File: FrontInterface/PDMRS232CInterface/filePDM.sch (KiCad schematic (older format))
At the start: 9 parts

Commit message: PCB Update
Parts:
- renumbered .1 to .?, BP_CAN_IN1 to BP_CAN_IN?, BP_CAN_OUT1 to BP_CAN_OUT?, BP_Power1 to BP_Power?, C13 to C?, C14 to C?, F1 to F?, R4 to R?, R3 to R?
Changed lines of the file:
@@
 EESchema Schematic File Version 4
-LIBS:RS232C Interface-cache
+LIBS:RS232CInterface-cache
 EELAYER 26 0
 EELAYER END
@@
 Connection ~ 3250 3200
 $Comp
-L RS232C-Interface-rescue:CAPACITOR0805-pdm_1-rev0-eagle-import C14
+L RS232C-Interface-rescue:CAPACITOR0805-pdm_1-rev0-eagle-import C?
 U 1 0 DE3531F169098DAB
 P 4750 3400
-F 0 "C14" H 4800 3405 59  0000 L BNN
+F 0 "C?" H 4800 3405 59  0000 L BNN
 F 1 "100n" H 4800 3235 59  0000 L BNN
 F 2 "RS232C-Interface+PDM:Capacitor0805" H 4750 3400 50  0001 C CNN
@@
 $EndComp
 $Comp
-L RS232C-Interface-rescue:RJ45-SOCKET-pdm_1-rev0-eagle-import BP_CAN_OUT1
+L RS232C-Interface-rescue:RJ45-SOCKET-pdm_1-rev0-eagle-import BP_CAN_OUT?
 U 1 0 EC4CBBF8C3190B6C
 P 5450 3300
-F 0 "BP_CAN_OUT1" H 5250 3800 59  0000 L BNN
+F 0 "BP_CAN_OUT?" H 5250 3800 59  0000 L BNN
 F 1 "J" H 5250 2880 59  0000 L BNN
 F 2 "RS232C-Interface+PDM:RJ45-PCB-SOCKET" H 5450 3300 50  0001 C CNN
@@
 $EndComp
 $Comp
-L RS232C-Interface-rescue:HEADER2X4_NORMAL-pdm_1-rev0-eagle-import .1
+L RS232C-Interface-rescue:HEADER2X4_NORMAL-pdm_1-rev0-eagle-import .?
 U 1 0 2E5E96F5F6EEC095
 P 2850 1500
-F 0 ".1" H 2670 1535 59  0000 R TNN
+F 0 ".?" H 2670 1535 59  0000 R TNN
 F 1 "2x4" H 2850 1500 50  0001 C CNN
 F 2 "RS232C-Interface+PDM:Pinheader" H 2850 1500 50  0001 C CNN
@@
 $EndComp
 $Comp
-L RS232C-Interface-rescue:HEADER2X4_NORMAL-pdm_1-rev0-eagle-import .1
+L RS232C-Interface-rescue:HEADER2X4_NORMAL-pdm_1-rev0-eagle-import .?
 U 2 0 2E5E96F5F6EEC099
 P 3250 1500
-F 0 ".1" H 3070 1535 59  0000 R TNN
+F 0 ".?" H 3070 1535 59  0000 R TNN
 F 1 "2x4" H 3250 1500 50  0001 C CNN
 F 2 "RS232C-Interface+PDM:Pinheader" H 3250 1500 50  0001 C CNN
@@
 $EndComp
 $Comp
-L RS232C-Interface-rescue:HEADER2X4_NORMAL-pdm_1-rev0-eagle-import .1
+L RS232C-Interface-rescue:HEADER2X4_NORMAL-pdm_1-rev0-eagle-import .?
 U 3 0 2E5E96F5F6EEC09D
 P 2850 2000
-F 0 ".1" H 2670 2035 59  0000 R TNN
+F 0 ".?" H 2670 2035 59  0000 R TNN
 F 1 "2x4" H 2850 2000 50  0001 C CNN
 F 2 "RS232C-Interface+PDM:Pinheader" H 2850 2000 50  0001 C CNN
@@
 $EndComp
 $Comp
-L RS232C-Interface-rescue:HEADER2X4_NORMAL-pdm_1-rev0-eagle-import .1
+L RS232C-Interface-rescue:HEADER2X4_NORMAL-pdm_1-rev0-eagle-import .?
 U 4 0 2E5E96F5F6EEC081
 P 3250 2000
-F 0 ".1" H 3070 2035 59  0000 R TNN
+F 0 ".?" H 3070 2035 59  0000 R TNN
 F 1 "2x4" H 3250 2000 50  0001 C CNN
 F 2 "RS232C-Interface+PDM:Pinheader" H 3250 2000 50  0001 C CNN
@@
 $EndComp
 $Comp
-L RS232C-Interface-rescue:HEADER2X4_NORMAL-pdm_1-rev0-eagle-import .1
+L RS232C-Interface-rescue:HEADER2X4_NORMAL-pdm_1-rev0-eagle-import .?
 U 5 0 2E5E96F5F6EEC085
 P 2850 2700
-F 0 ".1" H 2670 2735 59  0000 R TNN
+F 0 ".?" H 2670 2735 59  0000 R TNN
 F 1 "2x4" H 2850 2700 50  0001 C CNN
 F 2 "RS232C-Interface+PDM:Pinheader" H 2850 2700 50  0001 C CNN
@@
 $EndComp
 $Comp
-L RS232C-Interface-rescue:HEADER2X4_NORMAL-pdm_1-rev0-eagle-import .1
+L RS232C-Interface-rescue:HEADER2X4_NORMAL-pdm_1-rev0-eagle-import .?
 U 6 0 2E5E96F5F6EEC089
 P 3250 2700
-F 0 ".1" H 3070 2735 59  0000 R TNN
+F 0 ".?" H 3070 2735 59  0000 R TNN
 F 1 "2x4" H 3250 2700 50  0001 C CNN
 F 2 "RS232C-Interface+PDM:Pinheader" H 3250 2700 50  0001 C CNN
@@
 $EndComp
 $Comp
-L RS232C-Interface-rescue:HEADER2X4_NORMAL-pdm_1-rev0-eagle-import .1
+L RS232C-Interface-rescue:HEADER2X4_NORMAL-pdm_1-rev0-eagle-import .?
 U 7 0 2E5E96F5F6EEC08D
 P 2850 3200
-F 0 ".1" H 2670 3235 59  0000 R TNN
+F 0 ".?" H 2670 3235 59  0000 R TNN
 F 1 "2x4" H 2850 3200 50  0001 C CNN
 F 2 "RS232C-Interface+PDM:Pinheader" H 2850 3200 50  0001 C CNN
@@
 $EndComp
 $Comp
-L RS232C-Interface-rescue:HEADER2X4_NORMAL-pdm_1-rev0-eagle-import .1
+L RS232C-Interface-rescue:HEADER2X4_NORMAL-pdm_1-rev0-eagle-import .?
 U 8 0 2E5E96F5F6EEC0B1
 P 3250 3200
-F 0 ".1" H 3070 3235 59  0000 R TNN
+F 0 ".?" H 3070 3235 59  0000 R TNN
 F 1 "2x4" H 3250 3200 50  0001 C CNN
 F 2 "RS232C-Interface+PDM:Pinheader" H 3250 3200 50  0001 C CNN
@@
 $EndComp
 $Comp
-L RS232C-Interface-rescue:RESISTOR2010-pdm_1-rev0-eagle-import R3
+L RS232C-Interface-rescue:RESISTOR2010-pdm_1-rev0-eagle-import R?
 U 1 0 F977EDFF0ED61F71
 P 3050 1100
-F 0 "R3" H 2930 1245 59  0000 L BNN
+F 0 "R?" H 2930 1245 59  0000 L BNN
 F 1 "120R 0.25W" H 2930 1155 59  0000 L BNN
 F 2 "RS232C-Interface+PDM:Resistor-1206" H 3050 1100 50  0001 C CNN
@@
 $EndComp
 $Comp
-L RS232C-Interface-rescue:RESISTOR2010-pdm_1-rev0-eagle-import R4
+L RS232C-Interface-rescue:RESISTOR2010-pdm_1-rev0-eagle-import R?
 U 1 0 C80C4EE536D02DE4
 P 3050 3600
-F 0 "R4" H 2930 3645 59  0000 L BNN
+F 0 "R?" H 2930 3645 59  0000 L BNN
 F 1 "120R 0.25W" H 2930 3485 59  0000 L BNN
 F 2 "RS232C-Interface+PDM:Resistor-1206" H 3050 3600 50  0001 C CNN
@@
 $EndComp
 $Comp
-L RS232C-Interface-rescue:CAPACITOR0805-pdm_1-rev0-eagle-import C13
+L RS232C-Interface-rescue:CAPACITOR0805-pdm_1-rev0-eagle-import C?
 U 1 0 5902D293218CB388
 P 4700 2200
-F 0 "C13" H 4750 2205 59  0000 L BNN
+F 0 "C?" H 4750 2205 59  0000 L BNN
 F 1 "100n" H 4750 2035 59  0000 L BNN
 F 2 "RS232C-Interface+PDM:Capacitor0805" H 4700 2200 50  0001 C CNN
@@
 $EndComp
 $Comp
-L RS232C-Interface-rescue:TERMINAL-2-7.5X10.5MM-pdm_1-rev0-eagle-import BP_Power1
+L RS232C-Interface-rescue:TERMINAL-2-7.5X10.5MM-pdm_1-rev0-eagle-import BP_Power?
 U 1 0 6CFE1E7432EEE89C
 P 1400 2400
-F 0 "BP_Power1" V 1165 2600 59  0000 R TNN
+F 0 "BP_Power?" V 1165 2600 59  0000 R TNN
 F 1 "TERMINAL-2-2,5X5,5MM" H 1400 2400 50  0001 C CNN
 F 2 "RS232C-Interface+PDM:Screwterminal" H 1400 2400 50  0001 C CNN
@@
 Connection ~ 5050 2100
 $Comp
-L RS232C-Interface-rescue:RJ45-SOCKET-pdm_1-rev0-eagle-import BP_CAN_IN1
+L RS232C-Interface-rescue:RJ45-SOCKET-pdm_1-rev0-eagle-import BP_CAN_IN?
 U 1 0 647B296798085B15
 P 5450 2100
-F 0 "BP_CAN_IN1" H 5250 2600 59  0000 L BNN
+F 0 "BP_CAN_IN?" H 5250 2600 59  0000 L BNN
 F 1 "J" H 5250 1680 59  0000 L BNN
 F 2 "RS232C-Interface+PDM:RJ45-PCB-SOCKET" H 5450 2100 50  0001 C CNN
@@
 +24V
 $Comp
-L Device:Fuse F1
+L Device:Fuse F?
 U 1 1 5DCC2090
 P 1000 2550
-F 0 "F1" V 1060 2596 50  0000 L CNN
+F 0 "F?" V 1060 2596 50  0000 L CNN
 F 1 "Fuse" V 1060 2505 50  0000 R CNN
 F 2 "RS232C-Interface+PDM:Fuseholder" V 930 2550 50  0001 C CNN

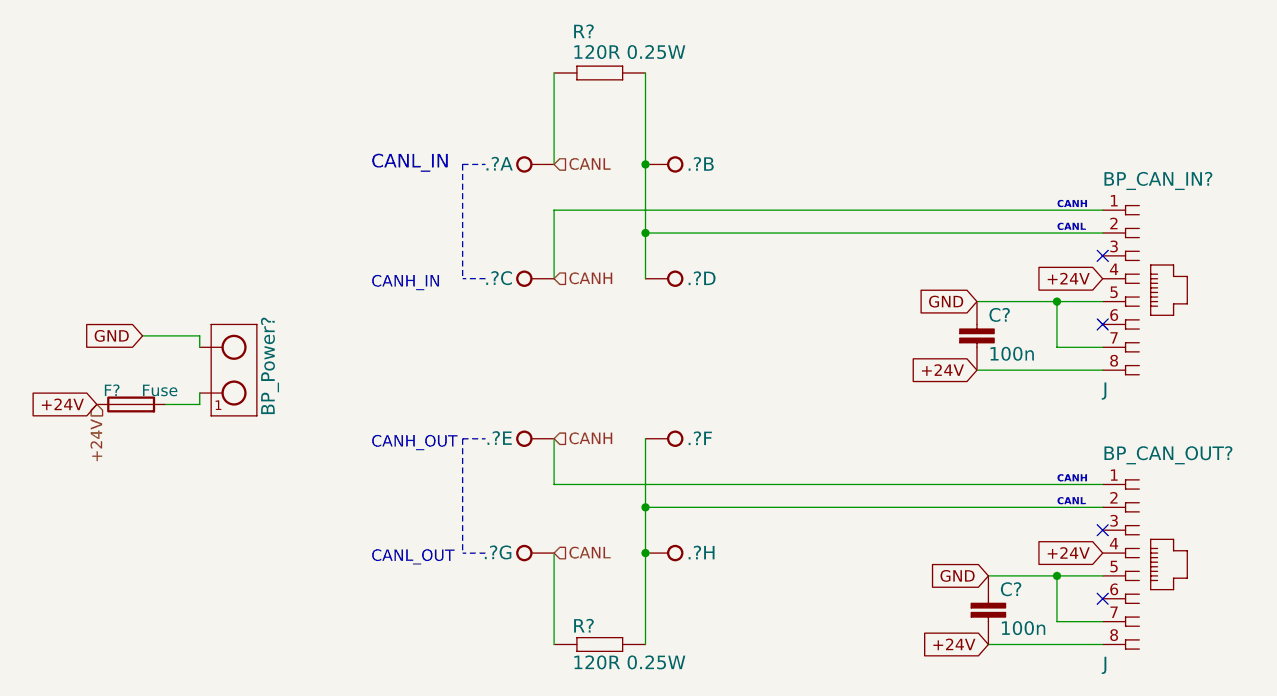
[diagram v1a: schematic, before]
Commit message: PCB updated, Lever Shifter added
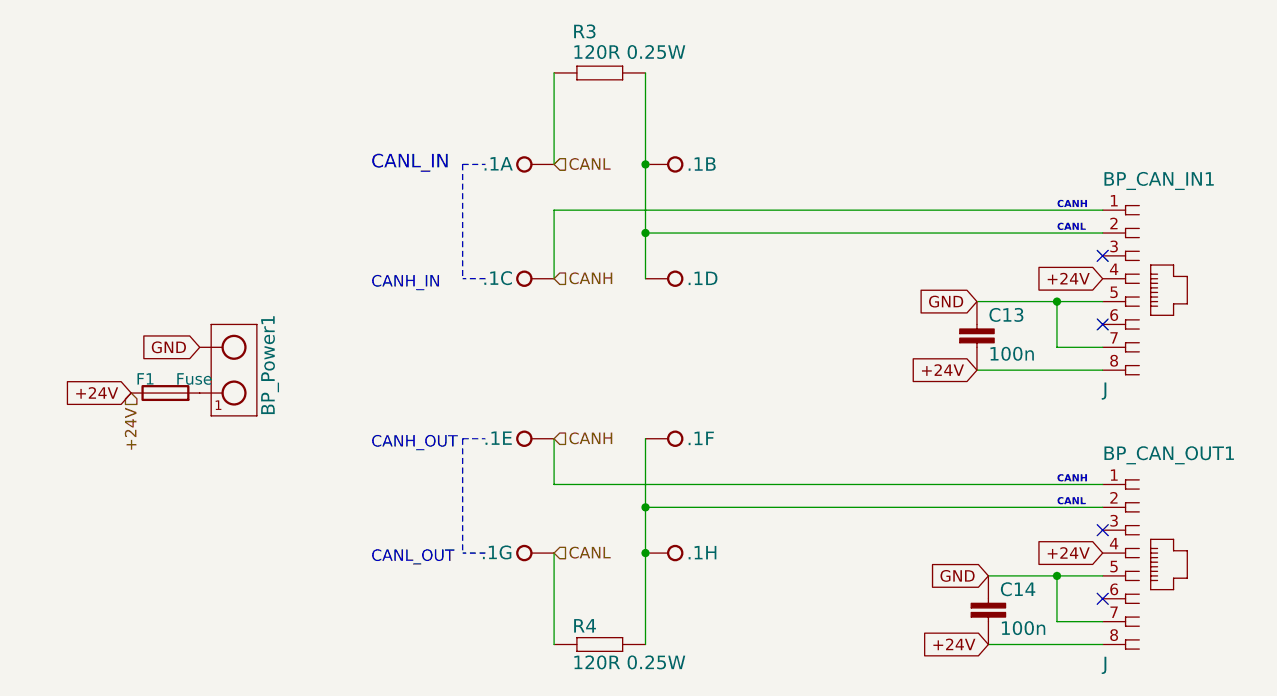
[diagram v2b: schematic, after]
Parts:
- removed .?: 2x4, RS232C-Interface+PDM:Pinheader, symbol RS232C-Interface-rescue:HEADER2X4_NORMAL-pdm_1-rev0-eagle-import
- added unit 3 of .1
- BP_CAN_IN1: renamed from BP_CAN_IN?; footprint RS232C-Interface+PDM:RJ45-PCB-SOCKET -> Connector_RJ:RJ45_Amphenol_54602-x08_Horizontal
- BP_CAN_OUT1: renamed from BP_CAN_OUT?; footprint RS232C-Interface+PDM:RJ45-PCB-SOCKET -> Connector_RJ:RJ45_Amphenol_54602-x08_Horizontal
- gave numbers to parts that had none: 7
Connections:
- net CANH: now also .1.3 (S)
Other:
- moved on the sheet: F1
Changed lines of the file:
@@
 Connection ~ 3250 3200
 $Comp
-L RS232C-Interface-rescue:CAPACITOR0805-pdm_1-rev0-eagle-import C?
+L RS232C-Interface-rescue:CAPACITOR0805-pdm_1-rev0-eagle-import C14
 U 1 0 DE3531F169098DAB
 P 4750 3400
-F 0 "C?" H 4800 3405 59  0000 L BNN
+F 0 "C14" H 4800 3405 59  0000 L BNN
 F 1 "100n" H 4800 3235 59  0000 L BNN
 F 2 "RS232C-Interface+PDM:Capacitor0805" H 4750 3400 50  0001 C CNN
@@
 $EndComp
 $Comp
-L RS232C-Interface-rescue:RJ45-SOCKET-pdm_1-rev0-eagle-import BP_CAN_OUT?
+L RS232C-Interface-rescue:RJ45-SOCKET-pdm_1-rev0-eagle-import BP_CAN_OUT1
 U 1 0 EC4CBBF8C3190B6C
 P 5450 3300
-F 0 "BP_CAN_OUT?" H 5250 3800 59  0000 L BNN
+F 0 "BP_CAN_OUT1" H 5250 3800 59  0000 L BNN
 F 1 "J" H 5250 2880 59  0000 L BNN
-F 2 "RS232C-Interface+PDM:RJ45-PCB-SOCKET" H 5450 3300 50  0001 C CNN
+F 2 "Connector_RJ:RJ45_Amphenol_54602-x08_Horizontal" H 5450 3300 50  0001 C CNN
 F 3 "https://de.rs-online.com/web/p/products/2400935/" H 5450 3300 50  0001 C CNN
 	1    5450 3300
@@
 $EndComp
 $Comp
-L RS232C-Interface-rescue:HEADER2X4_NORMAL-pdm_1-rev0-eagle-import .?
+L RS232C-Interface-rescue:HEADER2X4_NORMAL-pdm_1-rev0-eagle-import .1
 U 1 0 2E5E96F5F6EEC095
 P 2850 1500
-F 0 ".?" H 2670 1535 59  0000 R TNN
+F 0 ".1" H 2670 1535 59  0000 R TNN
 F 1 "2x4" H 2850 1500 50  0001 C CNN
 F 2 "RS232C-Interface+PDM:Pinheader" H 2850 1500 50  0001 C CNN
@@
 $EndComp
 $Comp
-L RS232C-Interface-rescue:HEADER2X4_NORMAL-pdm_1-rev0-eagle-import .?
+L RS232C-Interface-rescue:HEADER2X4_NORMAL-pdm_1-rev0-eagle-import .1
 U 2 0 2E5E96F5F6EEC099
 P 3250 1500
-F 0 ".?" H 3070 1535 59  0000 R TNN
+F 0 ".1" H 3070 1535 59  0000 R TNN
 F 1 "2x4" H 3250 1500 50  0001 C CNN
 F 2 "RS232C-Interface+PDM:Pinheader" H 3250 1500 50  0001 C CNN
@@
 $EndComp
 $Comp
-L RS232C-Interface-rescue:HEADER2X4_NORMAL-pdm_1-rev0-eagle-import .?
-U 3 0 2E5E96F5F6EEC09D
-P 2850 2000
-F 0 ".?" H 2670 2035 59  0000 R TNN
-F 1 "2x4" H 2850 2000 50  0001 C CNN
-F 2 "RS232C-Interface+PDM:Pinheader" H 2850 2000 50  0001 C CNN
-F 3 "https://de.rs-online.com/web/p/leiterplatten-header/8236434/" H 2850 2000 50  0001 C CNN
-	3    2850 2000
-	1    0    0    -1
-$EndComp
-$Comp
-L RS232C-Interface-rescue:HEADER2X4_NORMAL-pdm_1-rev0-eagle-import .?
+L RS232C-Interface-rescue:HEADER2X4_NORMAL-pdm_1-rev0-eagle-import .1
 U 4 0 2E5E96F5F6EEC081
 P 3250 2000
-F 0 ".?" H 3070 2035 59  0000 R TNN
+F 0 ".1" H 3070 2035 59  0000 R TNN
 F 1 "2x4" H 3250 2000 50  0001 C CNN
 F 2 "RS232C-Interface+PDM:Pinheader" H 3250 2000 50  0001 C CNN
@@
 $EndComp
 $Comp
-L RS232C-Interface-rescue:HEADER2X4_NORMAL-pdm_1-rev0-eagle-import .?
+L RS232C-Interface-rescue:HEADER2X4_NORMAL-pdm_1-rev0-eagle-import .1
 U 5 0 2E5E96F5F6EEC085
 P 2850 2700
-F 0 ".?" H 2670 2735 59  0000 R TNN
+F 0 ".1" H 2670 2735 59  0000 R TNN
 F 1 "2x4" H 2850 2700 50  0001 C CNN
 F 2 "RS232C-Interface+PDM:Pinheader" H 2850 2700 50  0001 C CNN
@@
 $EndComp
 $Comp
-L RS232C-Interface-rescue:HEADER2X4_NORMAL-pdm_1-rev0-eagle-import .?
+L RS232C-Interface-rescue:HEADER2X4_NORMAL-pdm_1-rev0-eagle-import .1
 U 6 0 2E5E96F5F6EEC089
 P 3250 2700
-F 0 ".?" H 3070 2735 59  0000 R TNN
+F 0 ".1" H 3070 2735 59  0000 R TNN
 F 1 "2x4" H 3250 2700 50  0001 C CNN
 F 2 "RS232C-Interface+PDM:Pinheader" H 3250 2700 50  0001 C CNN
@@
 $EndComp
 $Comp
-L RS232C-Interface-rescue:HEADER2X4_NORMAL-pdm_1-rev0-eagle-import .?
+L RS232C-Interface-rescue:HEADER2X4_NORMAL-pdm_1-rev0-eagle-import .1
 U 7 0 2E5E96F5F6EEC08D
 P 2850 3200
-F 0 ".?" H 2670 3235 59  0000 R TNN
+F 0 ".1" H 2670 3235 59  0000 R TNN
 F 1 "2x4" H 2850 3200 50  0001 C CNN
 F 2 "RS232C-Interface+PDM:Pinheader" H 2850 3200 50  0001 C CNN
@@
 $EndComp
 $Comp
-L RS232C-Interface-rescue:HEADER2X4_NORMAL-pdm_1-rev0-eagle-import .?
+L RS232C-Interface-rescue:HEADER2X4_NORMAL-pdm_1-rev0-eagle-import .1
 U 8 0 2E5E96F5F6EEC0B1
 P 3250 3200
-F 0 ".?" H 3070 3235 59  0000 R TNN
+F 0 ".1" H 3070 3235 59  0000 R TNN
 F 1 "2x4" H 3250 3200 50  0001 C CNN
 F 2 "RS232C-Interface+PDM:Pinheader" H 3250 3200 50  0001 C CNN
@@
 $EndComp
 $Comp
-L RS232C-Interface-rescue:RESISTOR2010-pdm_1-rev0-eagle-import R?
+L RS232C-Interface-rescue:RESISTOR2010-pdm_1-rev0-eagle-import R3
 U 1 0 F977EDFF0ED61F71
 P 3050 1100
-F 0 "R?" H 2930 1245 59  0000 L BNN
+F 0 "R3" H 2930 1245 59  0000 L BNN
 F 1 "120R 0.25W" H 2930 1155 59  0000 L BNN
 F 2 "RS232C-Interface+PDM:Resistor-1206" H 3050 1100 50  0001 C CNN
@@
 $EndComp
 $Comp
-L RS232C-Interface-rescue:RESISTOR2010-pdm_1-rev0-eagle-import R?
+L RS232C-Interface-rescue:RESISTOR2010-pdm_1-rev0-eagle-import R4
 U 1 0 C80C4EE536D02DE4
 P 3050 3600
-F 0 "R?" H 2930 3645 59  0000 L BNN
+F 0 "R4" H 2930 3645 59  0000 L BNN
 F 1 "120R 0.25W" H 2930 3485 59  0000 L BNN
 F 2 "RS232C-Interface+PDM:Resistor-1206" H 3050 3600 50  0001 C CNN
@@
 $EndComp
 $Comp
-L RS232C-Interface-rescue:CAPACITOR0805-pdm_1-rev0-eagle-import C?
+L RS232C-Interface-rescue:CAPACITOR0805-pdm_1-rev0-eagle-import C13
 U 1 0 5902D293218CB388
 P 4700 2200
-F 0 "C?" H 4750 2205 59  0000 L BNN
+F 0 "C13" H 4750 2205 59  0000 L BNN
 F 1 "100n" H 4750 2035 59  0000 L BNN
 F 2 "RS232C-Interface+PDM:Capacitor0805" H 4700 2200 50  0001 C CNN
@@
 	1    4700 2200
 	1    0    0    -1
-$EndComp
-$Comp
-L RS232C-Interface-rescue:TERMINAL-2-7.5X10.5MM-pdm_1-rev0-eagle-import BP_Power?
-U 1 0 6CFE1E7432EEE89C
-P 1400 2400
-F 0 "BP_Power?" V 1165 2600 59  0000 R TNN
-F 1 "TERMINAL-2-2,5X5,5MM" H 1400 2400 50  0001 C CNN
-F 2 "RS232C-Interface+PDM:Screwterminal" H 1400 2400 50  0001 C CNN
-F 3 "https://de.rs-online.com/web/p/products/2204260/" H 1400 2400 50  0001 C CNN
-	1    1400 2400
-	-1   0    0    1
 $EndComp
 Text Notes 2050 1530 0    59   ~ 0
@@
 Text GLabel 4700 2400 0    50   Input ~ 0
 +24V
-Text GLabel 1050 2250 0    50   Input ~ 0
+Text GLabel 1300 2300 0    50   Input ~ 0
 GND
-Text GLabel 850  2550 0    50   Input ~ 0
+Text GLabel 1000 2500 0    50   Input ~ 0
 +24V
 Text GLabel 5250 2000 0    50   Input ~ 0
@@
 Connection ~ 5050 2100
 $Comp
-L RS232C-Interface-rescue:RJ45-SOCKET-pdm_1-rev0-eagle-import BP_CAN_IN?
+L RS232C-Interface-rescue:RJ45-SOCKET-pdm_1-rev0-eagle-import BP_CAN_IN1
 U 1 0 647B296798085B15
 P 5450 2100
-F 0 "BP_CAN_IN?" H 5250 2600 59  0000 L BNN
+F 0 "BP_CAN_IN1" H 5250 2600 59  0000 L BNN
 F 1 "J" H 5250 1680 59  0000 L BNN
-F 2 "RS232C-Interface+PDM:RJ45-PCB-SOCKET" H 5450 2100 50  0001 C CNN
+F 2 "Connector_RJ:RJ45_Amphenol_54602-x08_Horizontal" H 5450 2100 50  0001 C CNN
 F 3 "https://de.rs-online.com/web/p/products/2400935/" H 5450 2100 50  0001 C CNN
 	1    5450 2100
@@
 Text GLabel 4750 3600 0    50   Input ~ 0
 +24V
-Text HLabel 850  2550 3    50   Input ~ 0
-+24V
-$Comp
-L Device:Fuse F?
+Text HLabel 1000 2500 3    50   Input ~ 0
++24V
+$Comp
+L Device:Fuse F1
 U 1 1 5DCC2090
-P 1000 2550
-F 0 "F?" V 1060 2596 50  0000 L CNN
-F 1 "Fuse" V 1060 2505 50  0000 R CNN
-F 2 "RS232C-Interface+PDM:Fuseholder" V 930 2550 50  0001 C CNN
-F 3 "https://de.rs-online.com/web/p/sicherungshalter-offen/7690149/?relevancy-data=636F3D3126696E3D4931384E525353746F636B4E756D626572266C753D656E266D6D3D6D61746368616C6C26706D3D5E2828282872737C5253295B205D3F293F285C647B337D5B5C2D5C735D3F5C647B332C347D5B705061415D3F29297C283235285C647B387D7C5C647B317D5C2D5C647B377D2929292426706F3D3126736E3D592673723D2673743D52535F53544F434B5F4E554D4245522677633D4E4F4E45267573743D37363930313439267374613D3736393031343926&searchHistory=%7B%22enabled%22%3Atrue%7D" H 1000 2550 50  0001 C CNN
-	1    1000 2550
+P 1150 2500
+F 0 "F1" V 1210 2546 50  0000 L CNN
+F 1 "Fuse" V 1210 2455 50  0000 R CNN
+F 2 "RS232C-Interface+PDM:Fuseholder" V 1080 2500 50  0001 C CNN
+F 3 "https://de.rs-online.com/web/p/sicherungshalter-offen/7690149/?relevancy-data=636F3D3126696E3D4931384E525353746F636B4E756D626572266C753D656E266D6D3D6D61746368616C6C26706D3D5E2828282872737C5253295B205D3F293F285C647B337D5B5C2D5C735D3F5C647B332C347D5B705061415D3F29297C283235285C647B387D7C5C647B317D5C2D5C647B377D2929292426706F3D3126736E3D592673723D2673743D52535F53544F434B5F4E554D4245522677633D4E4F4E45267573743D37363930313439267374613D3736393031343926&searchHistory=%7B%22enabled%22%3Atrue%7D" H 1150 2500 50  0001 C CNN
+	1    1150 2500
 	0    -1   -1   0
 $EndComp
-Wire Wire Line
-	1300 2300 1300 2250
-Wire Wire Line
-	1300 2250 1050 2250
-Wire Wire Line
-	1300 2500 1300 2550
-Wire Wire Line
-	1300 2550 1150 2550
+$Comp
+L RS232C-Interface-rescue:TERMINAL-2-7.5X10.5MM-pdm_1-rev0-eagle-import BP_Power1
+U 1 0 6CFE1E7432EEE89C
+P 1400 2400
+F 0 "BP_Power1" V 1165 2600 59  0000 R TNN
+F 1 "TERMINAL-2-2,5X5,5MM" H 1400 2400 50  0001 C CNN
+F 2 "RS232C-Interface+PDM:Screwterminal" H 1400 2400 50  0001 C CNN
+F 3 "https://de.rs-online.com/web/p/products/2204260/" H 1400 2400 50  0001 C CNN
+	1    1400 2400
+	-1   0    0    1
+$EndComp
+$Comp
+L RS232C-Interface-rescue:HEADER2X4_NORMAL-pdm_1-rev0-eagle-import .1
+U 3 0 5DC9C72F
+P 2850 2000
+F 0 ".1" H 2670 2035 59  0000 R TNN
+F 1 "2x4" H 2850 2000 50  0001 C CNN
+F 2 "RS232C-Interface+PDM:Pinheader" H 2850 2000 50  0001 C CNN
+F 3 "https://de.rs-online.com/web/p/leiterplatten-header/8236434/" H 2850 2000 50  0001 C CNN
+	3    2850 2000
+	1    0    0    -1
+$EndComp
 $EndSCHEMATC
